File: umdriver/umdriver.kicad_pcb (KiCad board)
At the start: 4 copper layers, 117.6 x 100 mm, 83 parts, among them J1 SWD, J2 Conn_01x08, J3 Isolated rs485, K1 SPST, Q1 Q_NMOS_GDS, SW1 SW_Reset, SW2 SW_Test, U1 STGIPQ8C60T, U2 NCP718, U3 ATSAMD21G18A-AUT, U4 ISO3088DW, U5 PSU, Y1 32.768

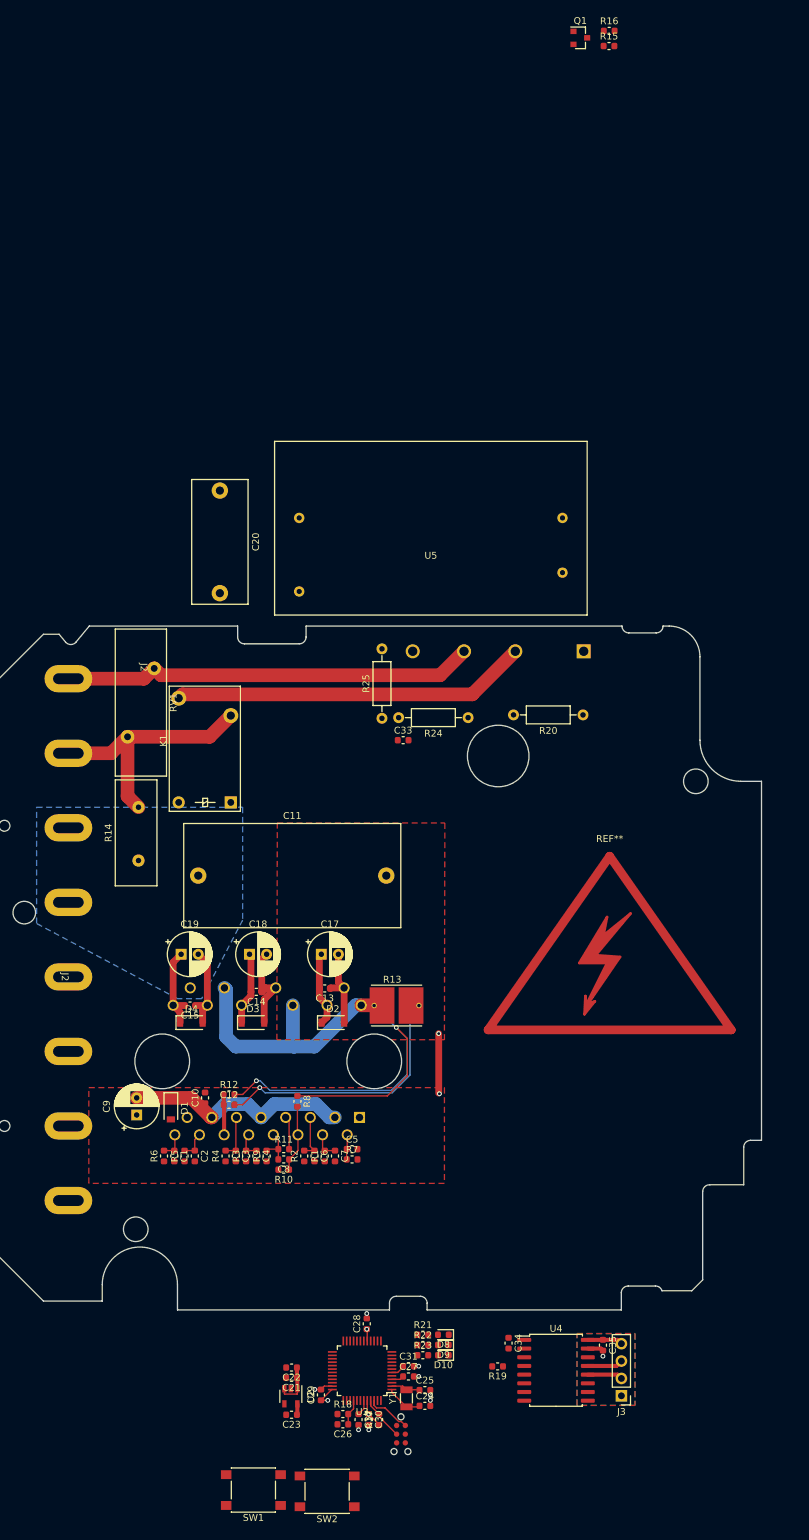
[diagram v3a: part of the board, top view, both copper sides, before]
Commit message: Try routing the MCU part
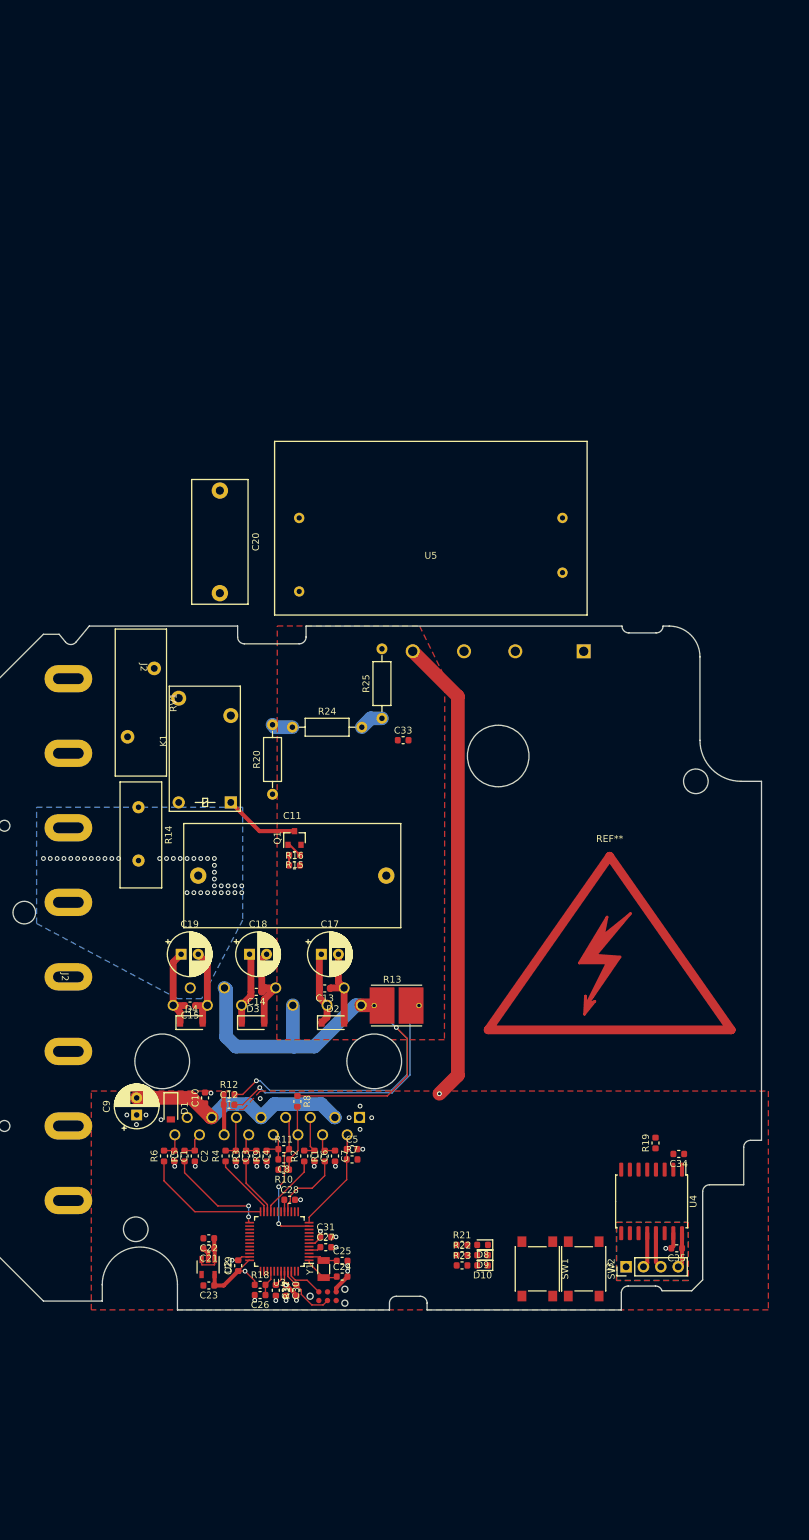
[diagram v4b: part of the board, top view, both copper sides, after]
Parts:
- moved R16 130.4 mm to (94.7, 75.0)
- moved R15 126.9 mm to (94.7, 73.5), turned to 180 degrees
- moved Q1 124.2 mm to (94.7, 71.0), turned to 90 degrees
- moved SW1 52.6 mm to (130.2, 134.0), turned to -90 degrees
- moved SW2 49.7 mm to (137.0, 134.0), turned to -90 degrees
- moved R20 46.9 mm to (91.5, 64.6), turned to 90 degrees
- moved R19 40.0 mm to (147.5, 115.6), turned to 90 degrees
- moved C34 37.2 mm to (150.9, 117.2), turned to 180 degrees
- moved U4 28.4 mm to (146.9, 124.1), turned to -90 degrees
- moved R24 25.7 mm to (94.4, 54.8), turned to 0 degrees
- moved U2 22.4 mm to (82.1, 133.7)
- moved C21 22.4 mm to (82.2, 131.0)
- moved C22 22.4 mm to (82.2, 129.5)
- moved C24 22.4 mm to (101.7, 135.1)
- moved C25 22.4 mm to (101.7, 132.8)
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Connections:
- Q1 pad 2: Net-(K1-PadA1) -> GND
- Q1 pad 3: GND -> Net-(K1-PadA1)
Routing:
- net GND: track 50.4 -> 115.1 mm, vias 11 -> 29
- net /LINE_N: track 60.3 -> 0.00 mm
- net Net-(D5-PadAC1): track 52.1 -> 18.4 mm
- net /LINU: track 0.00 -> 18.8 mm
- net /LINE_L: track 37.0 -> 19.7 mm
- net /ISENSE: track 4.85 -> 21.0 mm, vias 0 -> 2
- net /HINU: track 0.00 -> 15.5 mm, vias 0 -> 2
- net /NTC: track 3.63 -> 15.2 mm
- net Net-(K1-PadA1): track 0.00 -> 11.1 mm
- net /HINW: track 0.00 -> 10.8 mm
- net /LINV: track 0.00 -> 9.69 mm
- net /LINW: track 0.00 -> 9.39 mm
- net /HINV: track 0.00 -> 8.65 mm
- net +3V3: track 13.1 -> 21.6 mm, vias 3 -> 4
- net /DC_BUS_MON: track 0.00 -> 3.48 mm
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- added copper zone on In1.Cu, net +3V3
- added copper zone on In2.Cu, net /LINE_L
- added copper zone on In2.Cu, net /LINE_N
- added copper zone on In2.Cu, net GND
- added copper zone on In1.Cu, net Net-(D5-PadAC1)
- added copper zone on In1.Cu, net VBUS

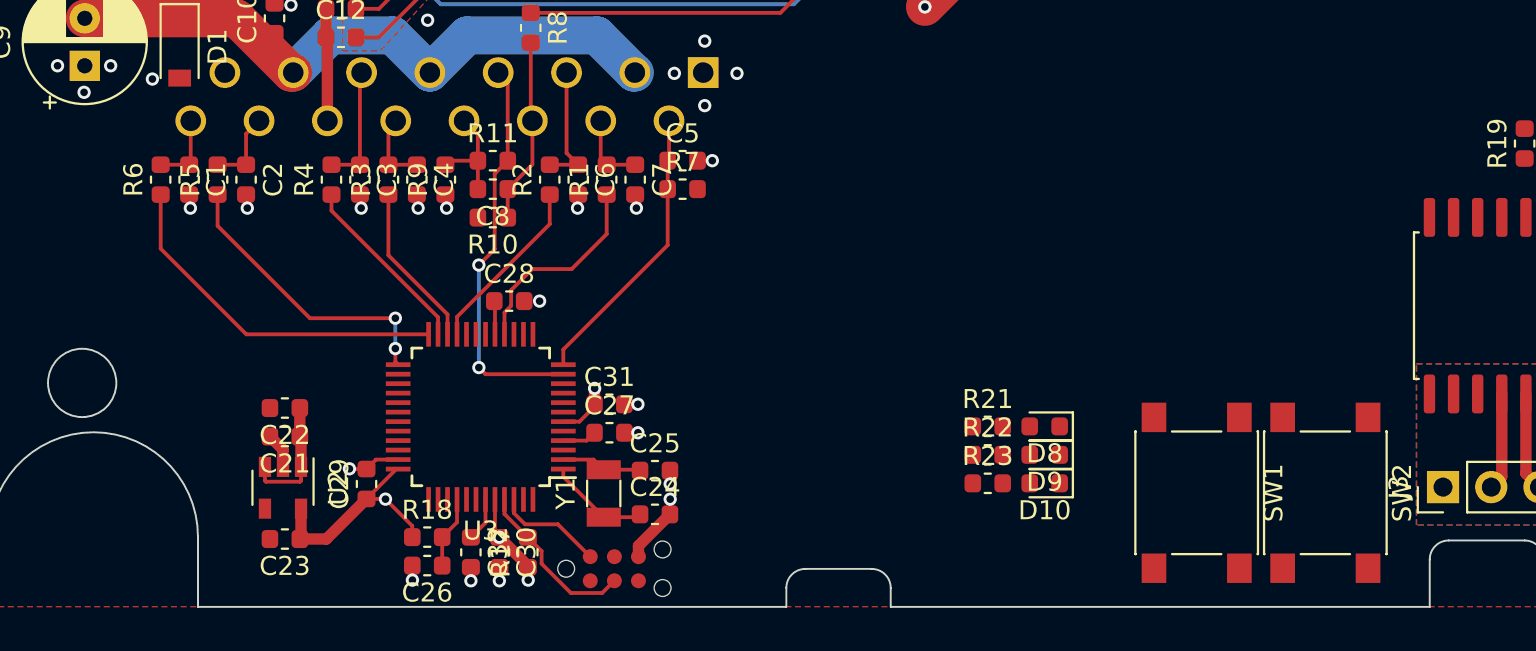
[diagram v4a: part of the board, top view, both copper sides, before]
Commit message: Route more MCU tracks
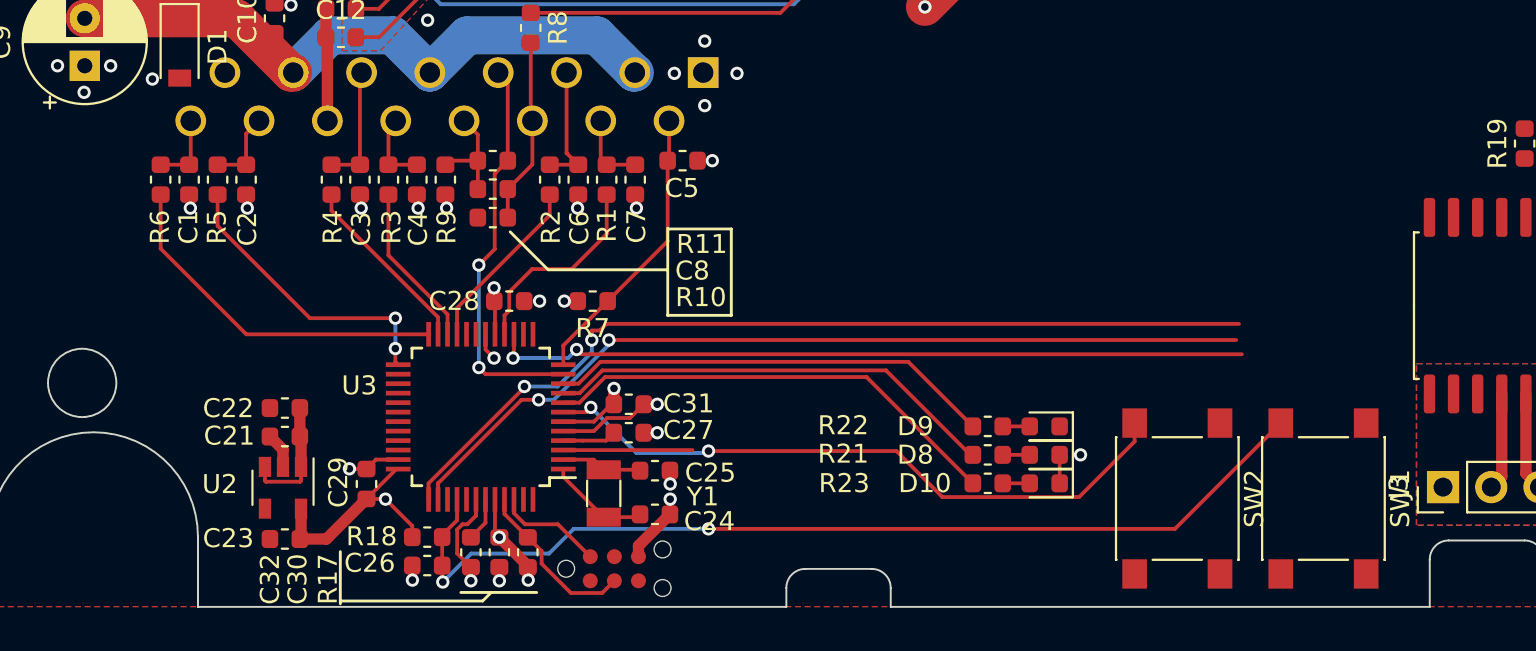
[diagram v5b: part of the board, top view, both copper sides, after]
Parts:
- moved SW2 7.81 mm to (129.2, 134.3)
- moved R7 7.57 mm to (98.4, 123.9), turned to 180 degrees
- moved SW1 6.69 mm to (136.9, 134.3)
- moved D8 1.50 mm to (122.2, 132.0)
- moved D9 1.50 mm to (122.2, 130.5)
- moved R21 1.50 mm to (119.2, 132.0)
- moved R22 1.50 mm to (119.2, 130.5)
- moved C27 1.02 mm to (100.3, 130.8)
- moved C31 1.02 mm to (100.3, 129.3)
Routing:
- net /Microcontroller/~MCU_RST: track 3.81 -> 52.3 mm, vias 0 -> 2
- net /Microcontroller/TX: track 0.00 -> 47.7 mm, vias 0 -> 2
- net /Microcontroller/RX: track 0.00 -> 46.2 mm, vias 0 -> 2
- net /Microcontroller/~RS485_RE: track 0.00 -> 40.0 mm, vias 0 -> 2
- net Net-(SW2-Pad2): track 0.00 -> 34.4 mm, vias 0 -> 2
- net /Microcontroller/LED3: track 0.00 -> 24.5 mm
- net /Microcontroller/LED1: track 0.00 -> 23.9 mm
- net /Microcontroller/LED2: track 0.00 -> 23.5 mm
- net GND: track 115.1 -> 127.3 mm, vias 29 -> 31
- net /DC_BUS_MON: track 3.48 -> 10.3 mm
- net +3V3: track 21.6 -> 23.5 mm, vias 4 -> 6
- net Net-(D9-Pad2): track 0.00 -> 1.42 mm
- net Net-(D8-Pad2): track 0.00 -> 1.42 mm
- net Net-(D10-Pad2): track 0.00 -> 1.42 mm
- net /Microcontroller/MCU_AREF: track 1.82 -> 2.83 mm

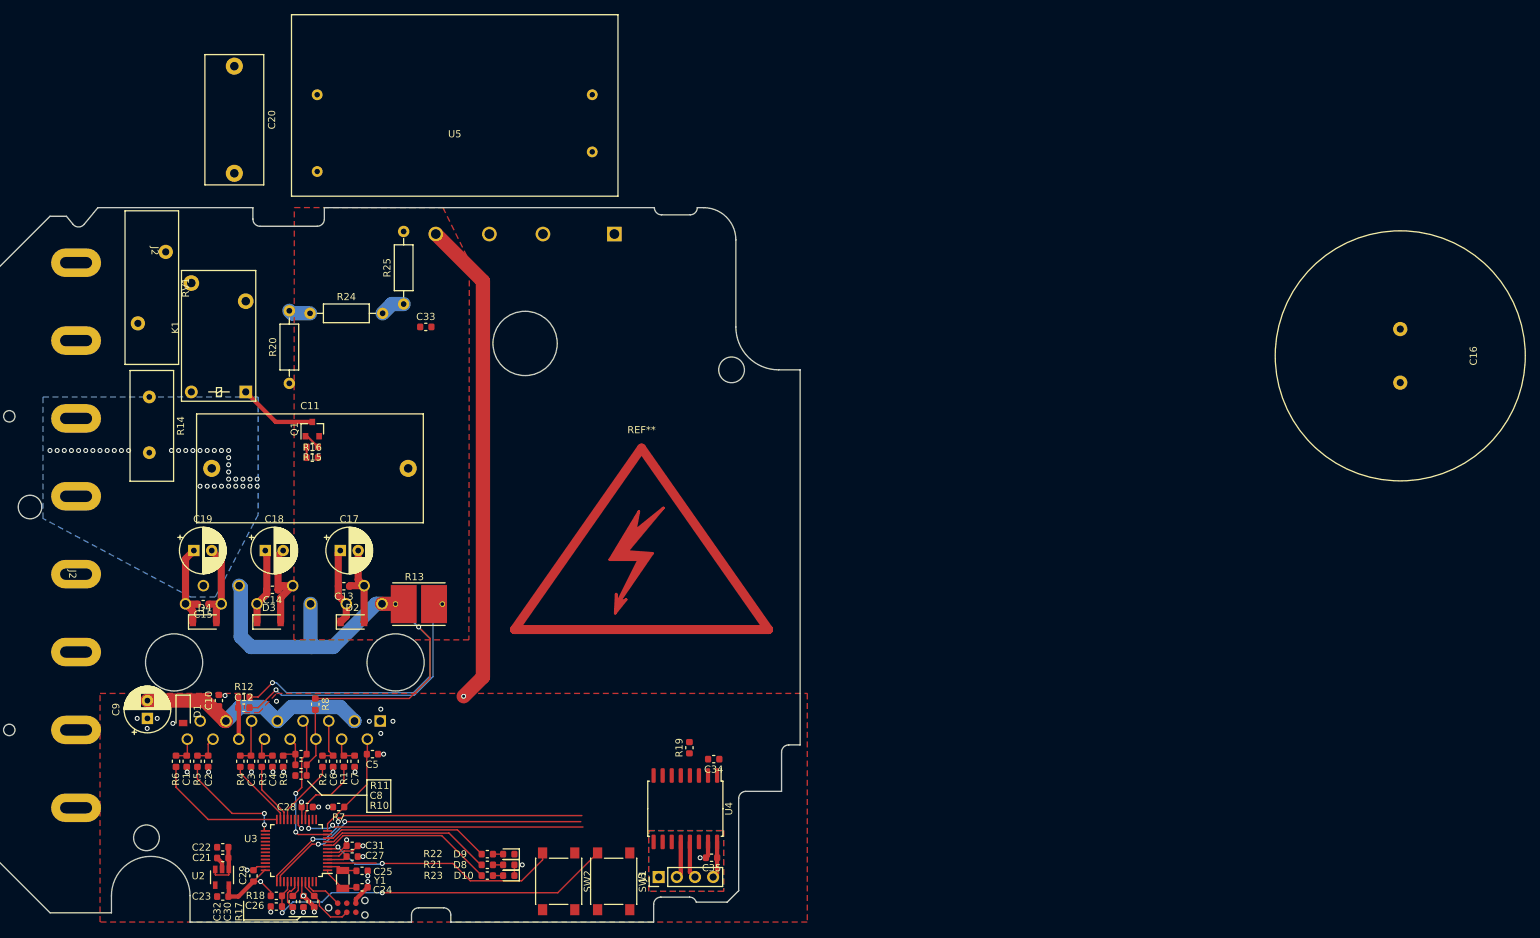
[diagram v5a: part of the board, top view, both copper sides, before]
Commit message: Main board routing complete
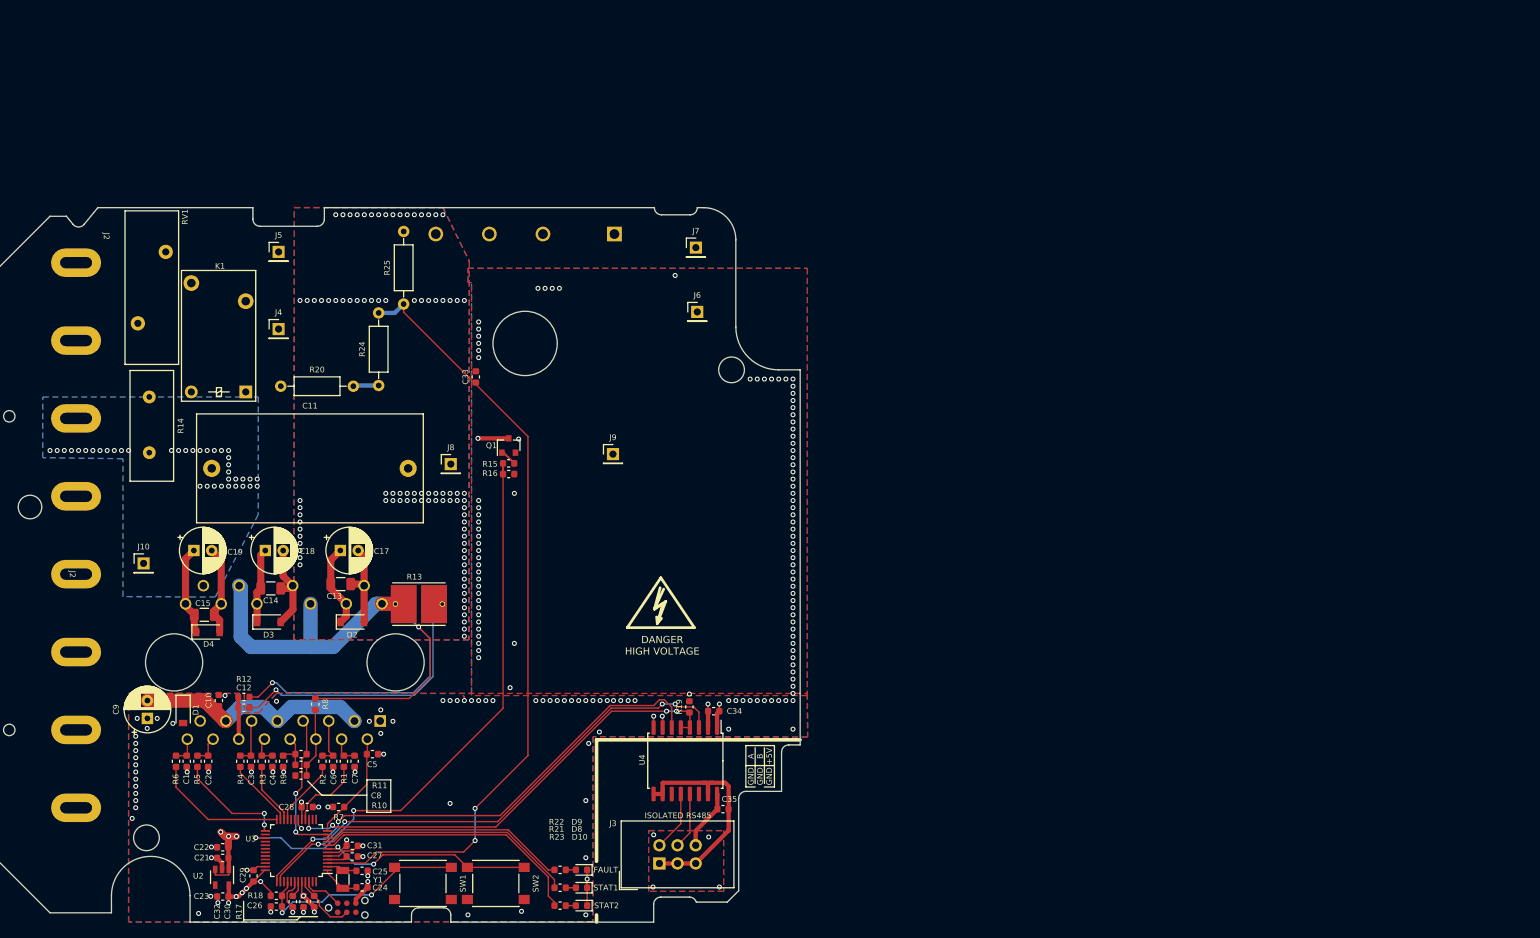
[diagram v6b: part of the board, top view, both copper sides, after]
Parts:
- removed C16: >9000, Capacitor_THT:C_Radial_D18.0mm_H35.5mm_P7.50mm
- removed C20: C, Capacitor_THT:C_Rect_L18.0mm_W8.0mm_P15.00mm_FKS3_FKP3
- removed REF**: Symbol_HighVoltage_Type2_CopperTop_Big, Symbols:Symbol_HighVoltage_Type2_CopperTop_Big
- removed U5: PSU, umdriver:IRM-10-15
- added J10: Conn_01x01, Pin_Headers:Pin_Header_Straight_1x01_Pitch2.54mm, F.Cu at (71.1, 89.8)
- added J4: Conn_01x01, Pin_Headers:Pin_Header_Straight_1x01_Pitch2.54mm, F.Cu at (90.0, 57.0)
- added J5: Conn_01x01, Pin_Headers:Pin_Header_Straight_1x01_Pitch2.54mm, F.Cu at (90.0, 46.2)
- added J6: Conn_01x01, Pin_Headers:Pin_Header_Straight_1x01_Pitch2.54mm, F.Cu at (148.6, 54.6)
- added J7: Conn_01x01, Pin_Headers:Pin_Header_Straight_1x01_Pitch2.54mm, F.Cu at (148.4, 45.6)
- added J8: Conn_01x01, Pin_Headers:Pin_Header_Straight_1x01_Pitch2.54mm, F.Cu at (114.1, 75.9)
- added J9: Conn_01x01, Pin_Headers:Pin_Header_Straight_1x01_Pitch2.54mm, F.Cu at (136.8, 74.5)
- added SYM1: SYM_Flash_Small, umdriver:Symbol_HighVoltage_Type2_Silkscreen_VerySmall, F.Cu at (143.5, 96.0)
- C13, C14, C15: footprint Capacitor_SMD:C_0603_1608Metric -> Capacitor_SMD:C_1206_3216Metric
- J3: footprint Pin_Headers:Pin_Header_Straight_1x04_Pitch2.54mm -> Connectors_IDC:IDC-Header_2x03_Pitch2.54mm_Straight
- moved Q1 27.6 mm to (122.2, 73.3)
- moved R15 27.6 mm to (122.2, 75.8)
- moved R16 27.6 mm to (122.2, 77.3)
- moved SW1 26.7 mm to (110.2, 134.6), turned to 180 degrees
- moved R24 13.9 mm to (104.0, 64.9), turned to 90 degrees
- moved D10 11.0 mm to (132.4, 137.7)
- moved R23 11.0 mm to (129.4, 137.7)
- moved D8 10.7 mm to (132.4, 135.2)
- moved R21 10.7 mm to (129.4, 135.2)
- moved D9 10.4 mm to (132.4, 132.7)
- moved R22 10.4 mm to (129.4, 132.7)
- moved C33 9.90 mm to (117.6, 63.7), turned to 90 degrees
- moved SW2 8.81 mm to (120.4, 134.6), turned to 180 degrees
- moved C35 6.99 mm to (152.2, 124.2), turned to 0 degrees
- moved C34 6.71 mm to (150.9, 110.5)
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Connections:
- J3 pad 3: /Microcontroller/ISO_B -> /Microcontroller/ISO_GND
- J3 pad 4: /Microcontroller/ISO_VCC -> /Microcontroller/ISO_B
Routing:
- net +15V: track 39.9 -> 379.5 mm, vias 0 -> 4
- net /DC_BUS_MON: track 10.3 -> 111.5 mm, vias 0 -> 2
- net /INRUSH_BYPASS: track 1.50 -> 79.7 mm, vias 0 -> 2
- net +3V3: track 23.5 -> 88.8 mm, vias 6 -> 11
- net GND: track 127.3 -> 70.7 mm, vias 31 -> 273
- net /Microcontroller/ISO_GND: track 2.33 -> 31.6 mm, vias 1 -> 3
- net Net-(K1-PadA1): track 11.1 -> 39.5 mm, vias 0 -> 1
- net /Microcontroller/RX: track 46.2 -> 72.2 mm, vias 2 -> 4
- net /Microcontroller/~RS485_RE: track 40.0 -> 65.1 mm, vias 2 -> 4
- net /Microcontroller/TX: track 47.7 -> 70.0 mm
- net /Microcontroller/~MCU_RST: track 52.3 -> 32.1 mm
- net /Microcontroller/LED3: track 24.5 -> 38.3 mm
- net /Microcontroller/LED1: track 23.9 -> 36.3 mm
- net /Microcontroller/LED2: track 23.5 -> 34.6 mm
- net Net-(SW2-Pad2): track 34.4 -> 29.9 mm
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- added copper zone on In1.Cu, net +15V
- added copper zone on B.Cu, net GND
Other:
- board text added: "A B +5V"
- board text added: "DANGER HIGH VOLTAGE"
- board text added: "FAULT"
- board text added: "GND GND GND"
- board text added: "ISOLATED RS485"
- board text added: "STAT1"
- board text added: "STAT2"
